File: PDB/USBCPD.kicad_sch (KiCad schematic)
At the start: 50 parts, among them J13 USB_C_Receptacle, Q10 STL6P3LLH6, Q9 STL6P3LLH6, U16 LM76005QRNPRQ1, U17 ST1S14PHR, U18 STUSB4700YQTR, U19 STR2P3LLH6, U20 INA228

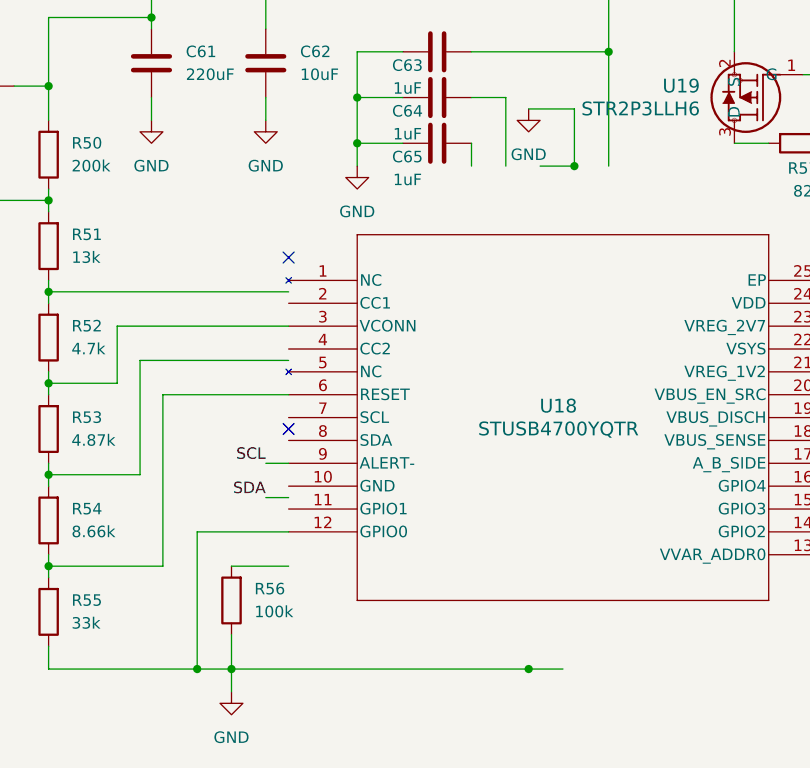
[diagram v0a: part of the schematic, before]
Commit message: removed battery oring
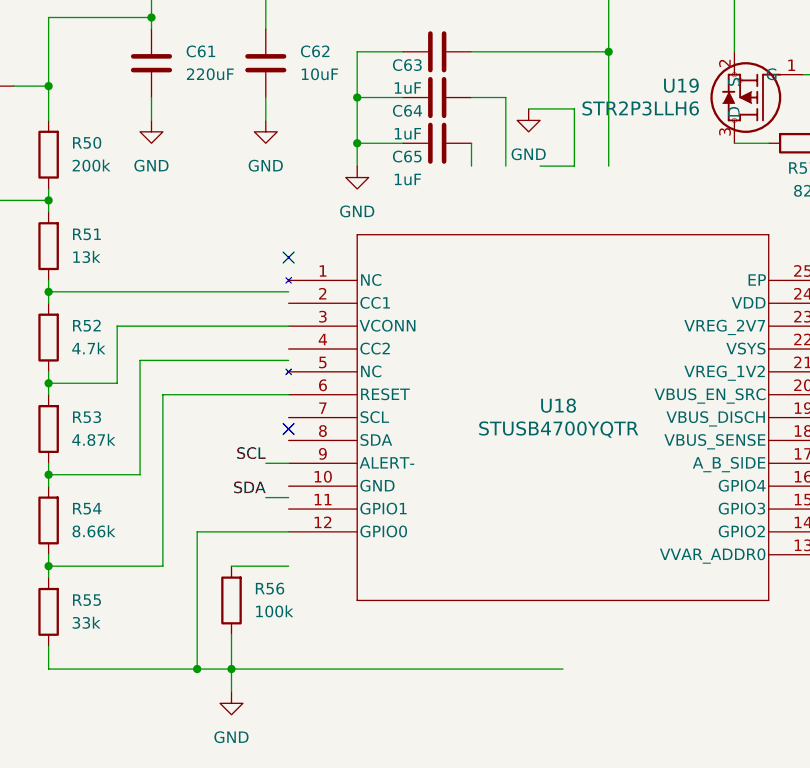
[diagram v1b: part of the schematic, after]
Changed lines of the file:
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@@
-	)
-	(junction
-		(at 359.41 234.95)
-		(diameter 0)
-		(color 0 0 0 0)
 	)
 	(junction
@@
 	(junction
 		(at 427.99 170.18)
-		(diameter 0)
-		(color 0 0 0 0)
-	)
-	(junction
-		(at 364.49 179.07)
 		(diameter 0)
 		(color 0 0 0 0)
@@
 	(wire
 		(pts
-			(xy 326.39 234.95) (xy 359.41 234.95)
+			(xy 326.39 234.95) (xy 363.22 234.95)
 		)
 		(stroke
@@
 		)
 		(stroke
-			(width 0)
-			(type default)
-		)
-	)
-	(wire
-		(pts
-			(xy 359.41 234.95) (xy 363.22 234.95)
-		)
-		(stroke

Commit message: did lots of routing
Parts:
- U16: footprint RNP0030A -> Dependencies:LM76005RNPR
- U17: footprint HSOP8_STM -> Dependencies:HSOP8_STM
- U18: footprint QFN_700QTR_STM -> Dependencies:QFN_700QTR_STM
- U19: footprint SOT_3LLH6_STM -> Dependencies:SOT_3LLH6_STM
- U20: footprint Package_SO:TSSOP-10_3x3mm_P0.5mm -> Package_SO:HVSSOP-10-1EP_3x3mm_P0.5mm_EP1.83x1.89mm
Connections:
- net +10VDC: now also U17.5 (EN2), U17.7 (VIN)
- net GND: now also U17.3 (*EN1), U17.6 (GND), U17.EPAD, U18.10 (GND), U18.22 (VSYS), U18.25 (EP), U18.3 (VCONN), U18.6 (RESET); no longer U18.12 (GPIO0)
- net SCL: now also U18.7 (SCL); no longer U18.9 (ALERT-)
- net SDA: now also U18.8 (SDA)
- net at C64.2: now also U18.21 (VREG_1V2)
- net at R52.1, R53.2: now also U18.14 (GPIO2); no longer U18.3 (VCONN)
- net at R51.1, R52.2: now also U18.15 (GPIO3)
- net at U18.24 (VDD): now also C60.1, C61.1, C62.1, C63.2, L6.2, Q9.D1 (D), R50.2, R58.2, U19.2 (S); no longer R60.1
- net at R54.1, R55.2: now also U18.12 (GPIO0); no longer U18.6 (RESET)
- net at R53.1, R54.2: now also U18.11 (GPIO1)
- net at C59.2: now also U17.1 (BOOT)
- net at C60.2, R50.1, R51.2: now also U17.4 (FB)
- net at U17.8 (SW): now also L6.1
- net at U18.13 (VVAR_ADDR0): now also R56.2
- net at J13.A5 (CC1): now also U18.2 (CC1); no longer U18.14 (GPIO2)
- net at U18.18 (VBUS_SENSE): now also F5.1, Q10.D1 (D)
- net at U18.19 (VBUS_DISCH): now also R58.1, U19.1 (G)
- net at U18.20 (VBUS_EN_SRC): now also R60.1
- net at U18.23 (VREG_2V7): now also C65.2
- net at U18.4 (CC2): now also J13.B5 (CC2)
- net at R61.4, R62.1, TP10.1: now also J13.A4 (VBUS)
- net at J13.A9 (VBUS), J13.B4 (VBUS), J13.B9 (VBUS): no longer J13.A4 (VBUS)
- net at R61.2: now also U20.10 (Vin+)
- net at R61.3: now also U20.9 (Vin-)
